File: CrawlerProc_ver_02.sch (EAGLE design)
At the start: 57 parts, among them U1 MIC5335-SPYMT, U10 ECS-160-8, U11 ANTENNA, U12 ANTENNA-CHIP, U2 MIC5320-JGYML, U3 ITG-3200, U4 AT86RF231-ZU, U5 AT45DB321D, U6 ECS-2033, U8 ADXL345-LGA12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

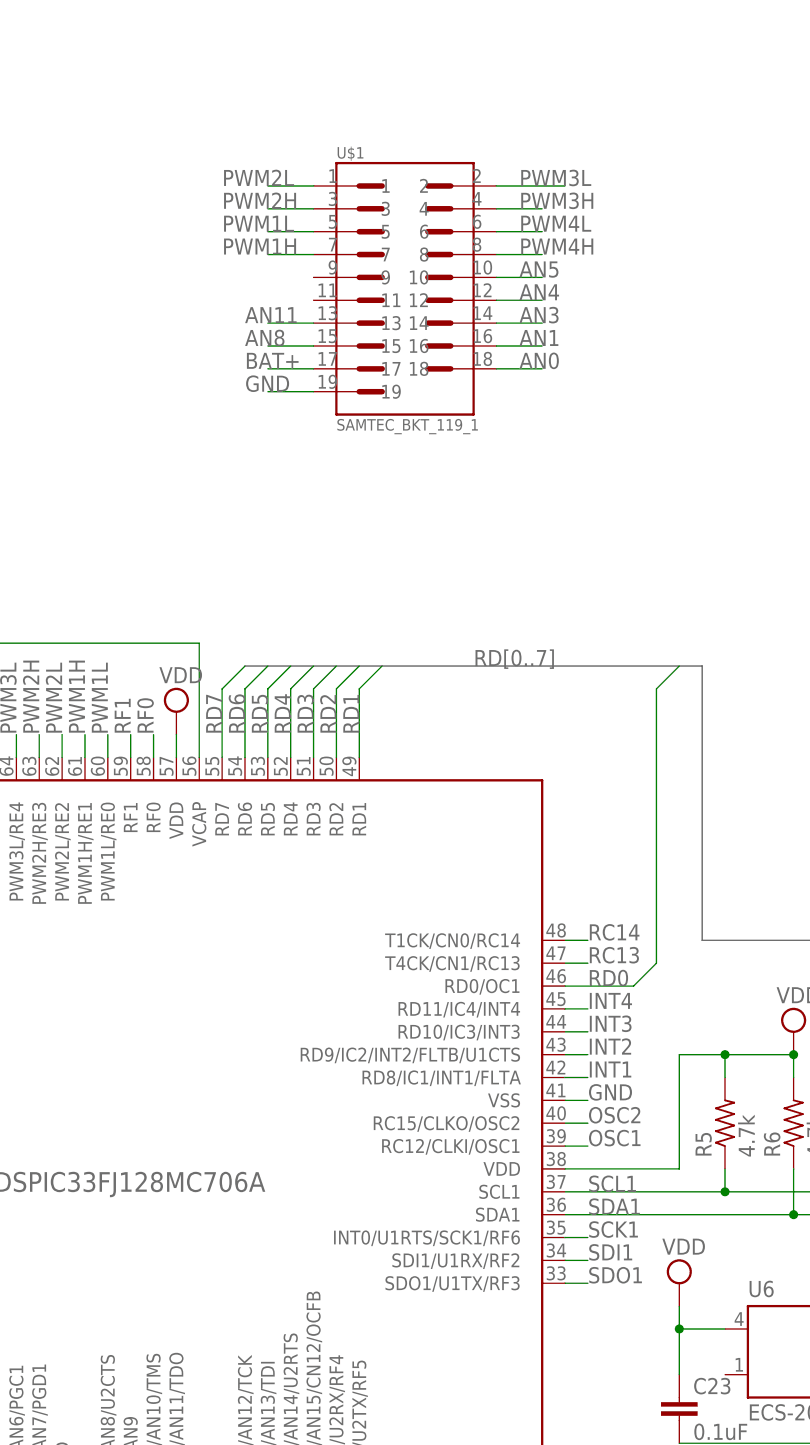
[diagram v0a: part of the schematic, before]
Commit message: Change 02 Schematic to have SPI pinout
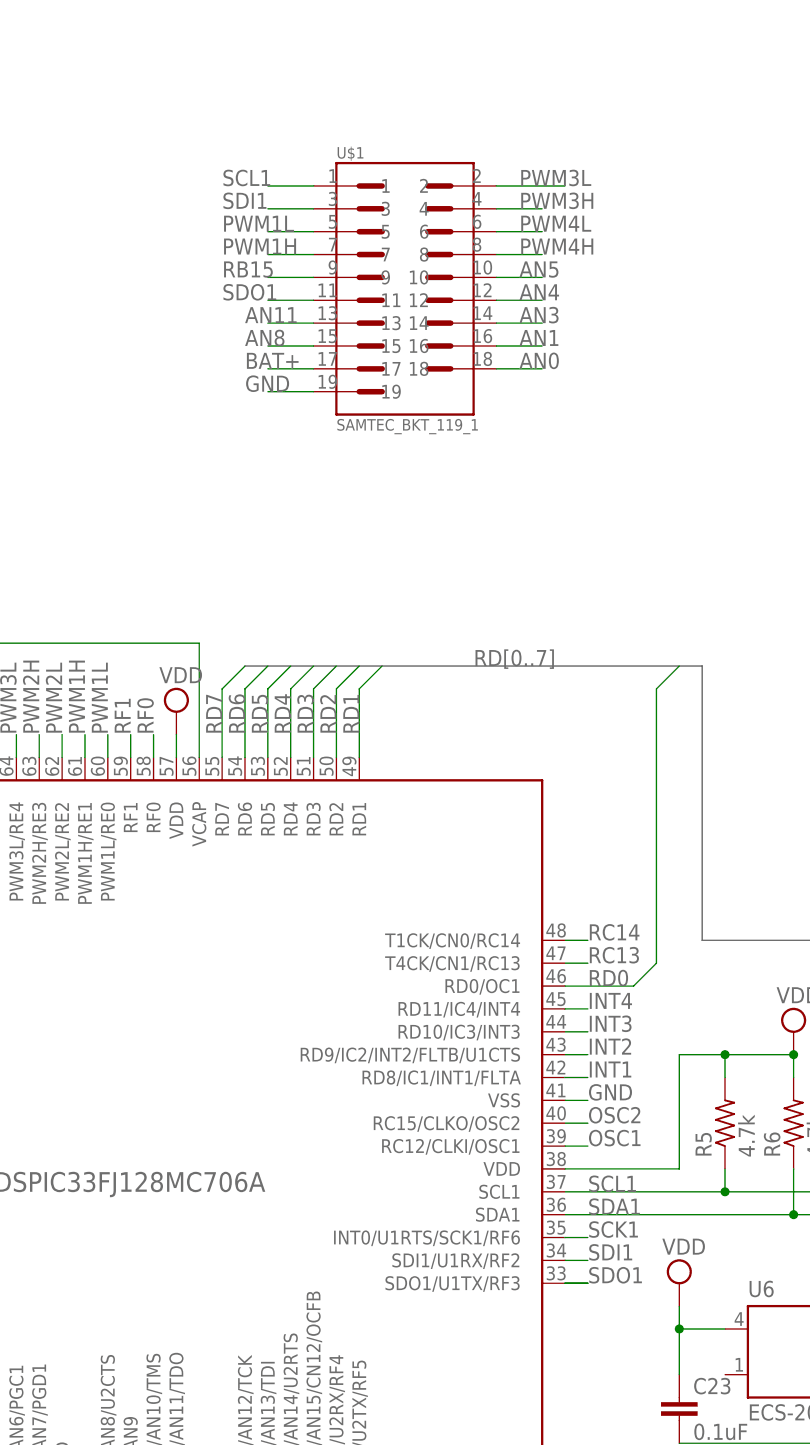
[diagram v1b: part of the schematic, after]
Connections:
- net PWM2H: no longer U$1.3
- net PWM2L: no longer U$1.1
- net RB15: now also U$1.9
- net SCL1: now also U$1.1
- net SDI1: now also U$1.3
- net SDO1: now also U$1.11
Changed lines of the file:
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@@
 <class number="0" name="default" width="0" drill="0">
 </class>
-<class number="1" name="sup" width="0.254" drill="0">
+<class number="1" name="sup" width="0.127" drill="0">
 </class>
 </classes>
@@
 <pinref part="U8" gate="G$1" pin="SCL"/>
 </segment>
+<segment>
+<pinref part="U$1" gate="G$1" pin="1"/>
+<wire x1="127" y1="187.96" x2="121.92" y2="187.96" width="0.1524" layer="91"/>
+<label x="116.84" y="187.96" size="1.778" layer="95"/>
+</segment>
 </net>
 <net name="SDA1" class="0">
@@
 <pinref part="U4" gate="G$1" pin="MISO"/>
 </segment>
+<segment>
+<pinref part="U$1" gate="G$1" pin="3"/>
+<wire x1="127" y1="185.42" x2="121.92" y2="185.42" width="0.1524" layer="91"/>
+<label x="116.84" y="185.42" size="1.778" layer="95"/>
+</segment>
 </net>
 <net name="SDO1" class="0">
@@
 <label x="157.48" y="66.04" size="1.778" layer="95"/>
 <pinref part="PROC" gate="G$1" pin="SDO1/U1TX/RF3"/>
+<wire x1="157.48" y1="66.04" x2="154.94" y2="66.04" width="0.1524" layer="91"/>
 </segment>
 <segment>
@@
 <label x="252.476" y="161.798" size="1.778" layer="95" rot="R180"/>
 <pinref part="U4" gate="G$1" pin="MOSI"/>
+</segment>
+<segment>
+<pinref part="U$1" gate="G$1" pin="11"/>
+<wire x1="127" y1="175.26" x2="121.92" y2="175.26" width="0.1524" layer="91"/>
+<label x="116.84" y="175.26" size="1.778" layer="95"/>
 </segment>
 </net>
@@
 <pinref part="U4" gate="G$1" pin="SLP_TR"/>
 </segment>
+<segment>
+<pinref part="U$1" gate="G$1" pin="9"/>
+<wire x1="127" y1="177.8" x2="121.92" y2="177.8" width="0.1524" layer="91"/>
+<label x="116.84" y="177.8" size="1.778" layer="95"/>
+</segment>
 </net>
 <net name="N$6" class="0">
@@
 <pinref part="PROC" gate="G$1" pin="PWM2H/RE3"/>
 </segment>
-<segment>
-<wire x1="127" y1="185.42" x2="121.92" y2="185.42" width="0.2032" layer="91"/>
-<label x="116.84" y="185.42" size="1.778" layer="95"/>
-<pinref part="U$1" gate="G$1" pin="3"/>
-</segment>
 </net>
 <net name="PWM1H" class="0">
@@
 <pinref part="PROC" gate="G$1" pin="PWM2L/RE2"/>
 </segment>
-<segment>
-<wire x1="127" y1="187.96" x2="121.92" y2="187.96" width="0.2032" layer="91"/>
-<label x="116.84" y="187.96" size="1.778" layer="95"/>
-<pinref part="U$1" gate="G$1" pin="1"/>
-</segment>
-</net>
+</net>
